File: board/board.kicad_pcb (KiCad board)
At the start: 4 copper layers, 100 x 100 mm, 52 parts, among them J1 UART, J2 USB_B, Q2 Q_NPN_BEC, SW1 SW_SPST, SW2 SW_SPST, SW4 SW_SPST, U1 4040, U2 NE555D, U3 4040, U4 LM741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

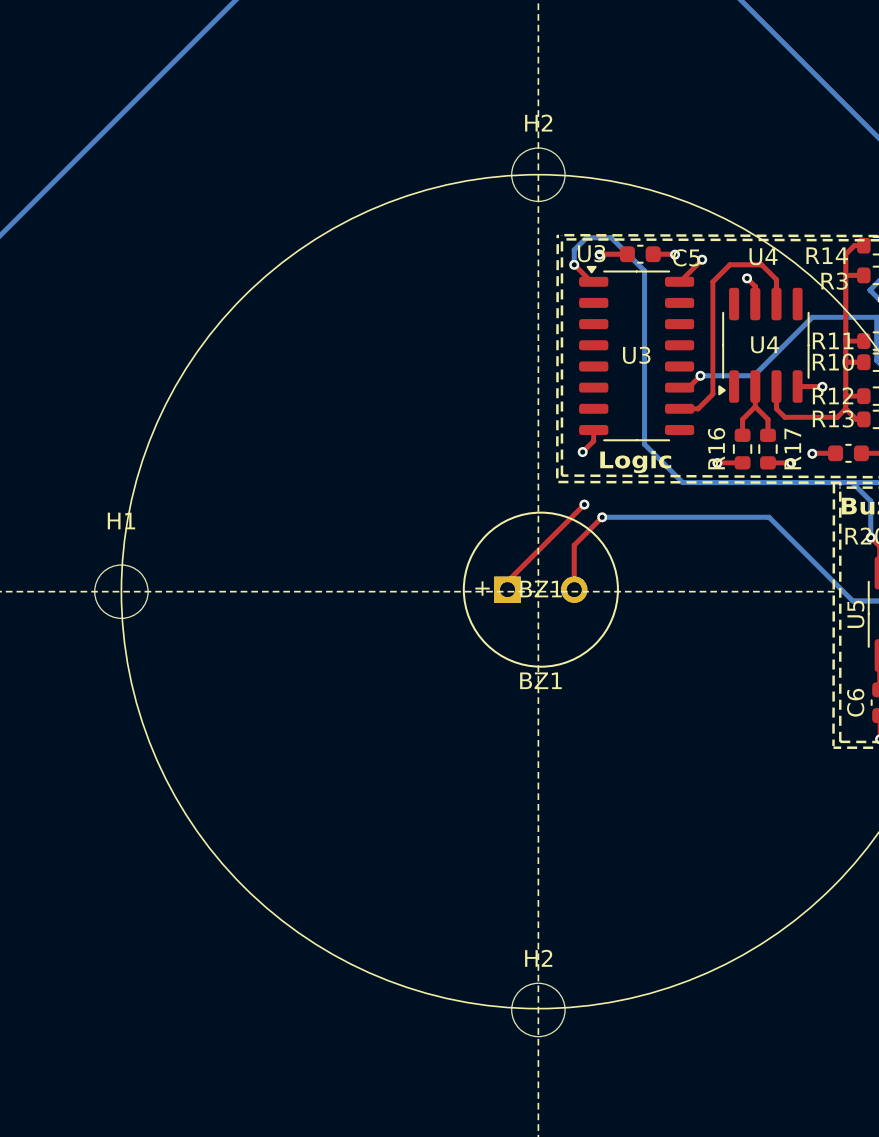
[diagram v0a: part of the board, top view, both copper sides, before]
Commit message: add: 9mm 3d push btn, VCC GND pins (battery)
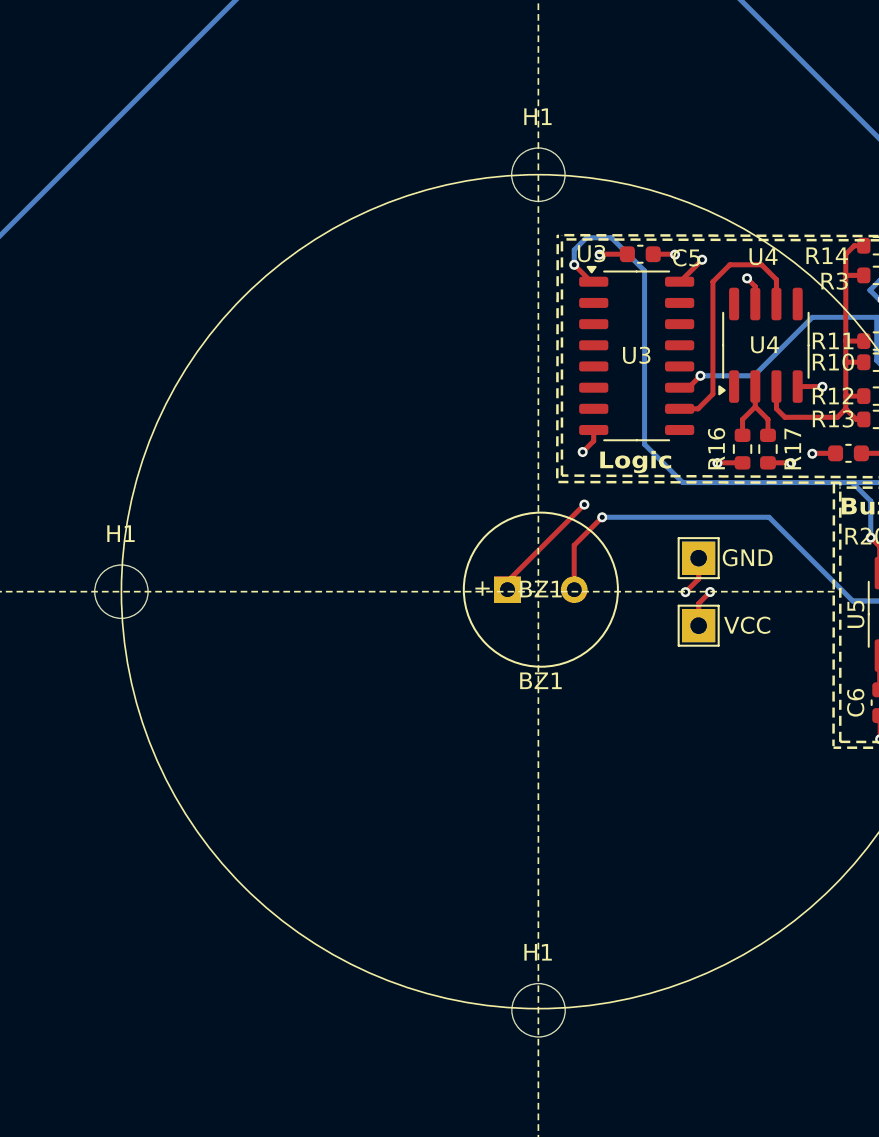
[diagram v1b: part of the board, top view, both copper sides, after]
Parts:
- removed H2 (x2): MountingHole, MountingHole:MountingHole_3.2mm_M3
- added GND: TestPoint, TestPoint:TestPoint_THTPad_2.0x2.0mm_Drill1.0mm, F.Cu at (80.5, 66.6)
- added H1: MountingHole, MountingHole:MountingHole_3.2mm_M3, F.Cu at (70.9, 93.7)
- added H1: MountingHole, MountingHole:MountingHole_3.2mm_M3, F.Cu at (70.8, 43.6)
- added VCC: TestPoint, TestPoint:TestPoint_THTPad_2.0x2.0mm_Drill1.0mm, F.Cu at (80.5, 70.7)
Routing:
- net GND: track 52.8 -> 55.2 mm, vias 31 -> 32
- net 5V: track 85.1 -> 87.4 mm, vias 26 -> 27

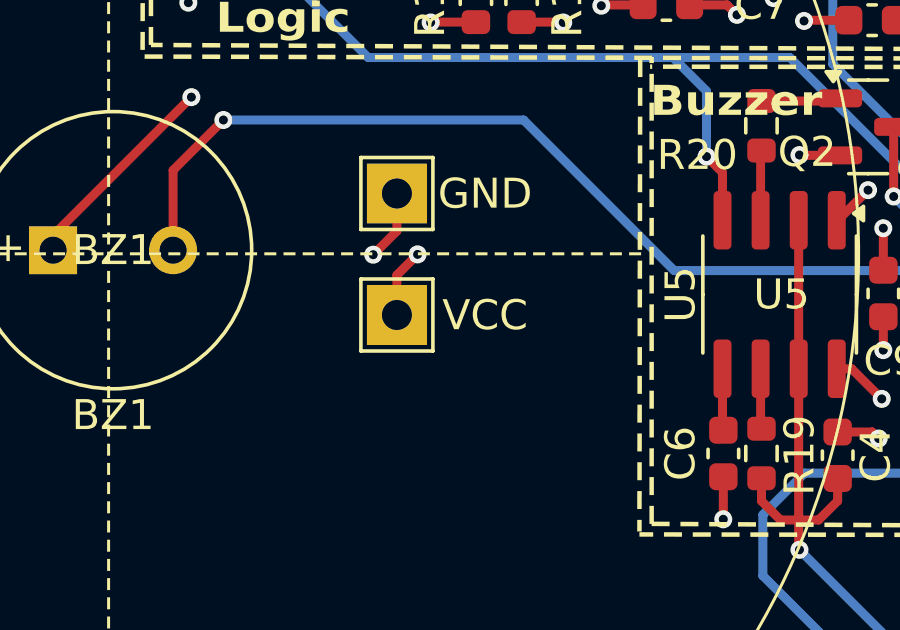
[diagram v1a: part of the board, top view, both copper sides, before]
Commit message: add: rectangle TIP GNS
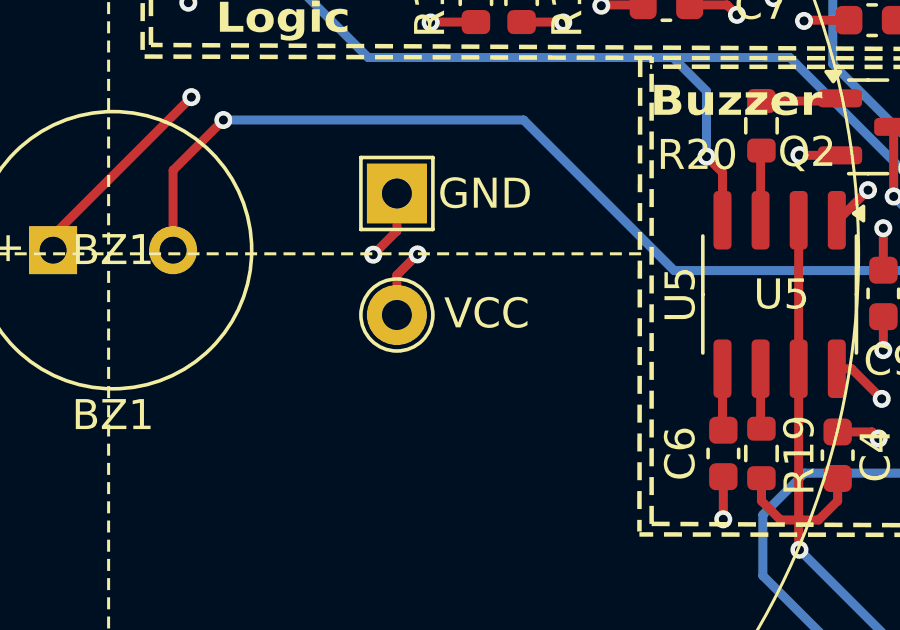
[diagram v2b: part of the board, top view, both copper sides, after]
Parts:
- VCC: footprint TestPoint:TestPoint_THTPad_2.0x2.0mm_Drill1.0mm -> TestPoint:TestPoint_THTPad_D2.0mm_Drill1.0mm
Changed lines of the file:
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@@
 		)
 	)
-	(footprint "TestPoint:TestPoint_THTPad_2.0x2.0mm_Drill1.0mm"
+	(footprint "TestPoint:TestPoint_THTPad_D2.0mm_Drill1.0mm"
 		(layer "F.Cu")
 		(at 80.46 70.66)
-		(descr "THT rectangular pad as test Point, square 2.0mm_Drill1.0mm  side length, hole diameter 1.0mm")
-		(tags "test point THT pad rectangle square")
+		(descr "THT pad as test Point, diameter 2.0mm, hole diameter 1.0mm")
+		(tags "test point THT pad")
 		(property "Reference" "VCC"
-			(at 2.94 0.01 0)
+			(at 3 -0.05 0)
 			(layer "F.SilkS")
 			(effects
@@
 		(sheetfile "board.kicad_sch")
 		(attr exclude_from_pos_files)
-		(fp_line
-			(start -1.2 -1.2)
-			(end 1.2 -1.2)
+		(fp_circle
+			(center 0 0)
+			(end 0 1.2)
 			(stroke
 				(width 0.12)
 				(type solid)
 			)
+			(fill no)
 			(layer "F.SilkS")
 		)
-		(fp_line
-			(start -1.2 1.2)
-			(end -1.2 -1.2)
-			(stroke
-				(width 0.12)
-				(type solid)
-			)
-			(layer "F.SilkS")
-		)
-		(fp_line
-			(start 1.2 -1.2)
-			(end 1.2 1.2)
-			(stroke
-				(width 0.12)
-				(type solid)
-			)
-			(layer "F.SilkS")
-		)
-		(fp_line
-			(start 1.2 1.2)
-			(end -1.2 1.2)
-			(stroke
-				(width 0.12)
-				(type solid)
-			)
-			(layer "F.SilkS")
-		)
-		(fp_line
-			(start -1.5 -1.5)
-			(end -1.5 1.5)
+		(fp_circle
+			(center 0 0)
+			(end 1.5 0)
 			(stroke
 				(width 0.05)
 				(type solid)
 			)
-			(layer "F.CrtYd")
-		)
-		(fp_line
-			(start -1.5 -1.5)
-			(end 1.5 -1.5)
-			(stroke
-				(width 0.05)
-				(type solid)
-			)
-			(layer "F.CrtYd")
-		)
-		(fp_line
-			(start 1.5 1.5)
-			(end -1.5 1.5)
-			(stroke
-				(width 0.05)
-				(type solid)
-			)
-			(layer "F.CrtYd")
-		)
-		(fp_line
-			(start 1.5 1.5)
-			(end 1.5 -1.5)
-			(stroke
-				(width 0.05)
-				(type solid)
-			)
+			(fill no)
 			(layer "F.CrtYd")
 		)
@@
 			)
 		)
-		(pad "1" thru_hole rect
+		(pad "1" thru_hole circle
 			(at 0 0)
 			(size 2 2)
